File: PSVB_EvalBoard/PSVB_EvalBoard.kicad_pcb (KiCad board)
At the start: 4 copper layers, 190 x 125 mm, 453 parts, among them J10 PIN20, J11 PIN12_2x6, J12 PIN20, J13 PIN6_2x3, J2 PIN2, J29 PIN6_2x3, J3 PIN20, J30 PIN6_2x3, J31 PIN6_2x3, J4 PIN20, J5 PIN20, J6 PIN20, J7 PIN20, J8 PIN20, J9 PIN20, Q1 S9013, U1 SGM2036-ADJ, U11 93LC56BT-IOT, U12 STM32F429ZETx, U13 CH395Q, U14 CH395Q, U15 24LC64ISN, U16 MPU6050, U17 W25Q128JVSIQ, U2 SGM2036-ADJ, U3 SGM2036-ADJ, U4 INA240A1PWR, U5 INA240A1PWR, U6 TM7707, U7 REF3030, U8 REF3025, U9 REF3012, X1 2.4576Mhz, X2 12Mhz_Passive_3225, X3 16Mhz_Passive_3225, X4 30Mhz_3225, X5 30Mhz_3225

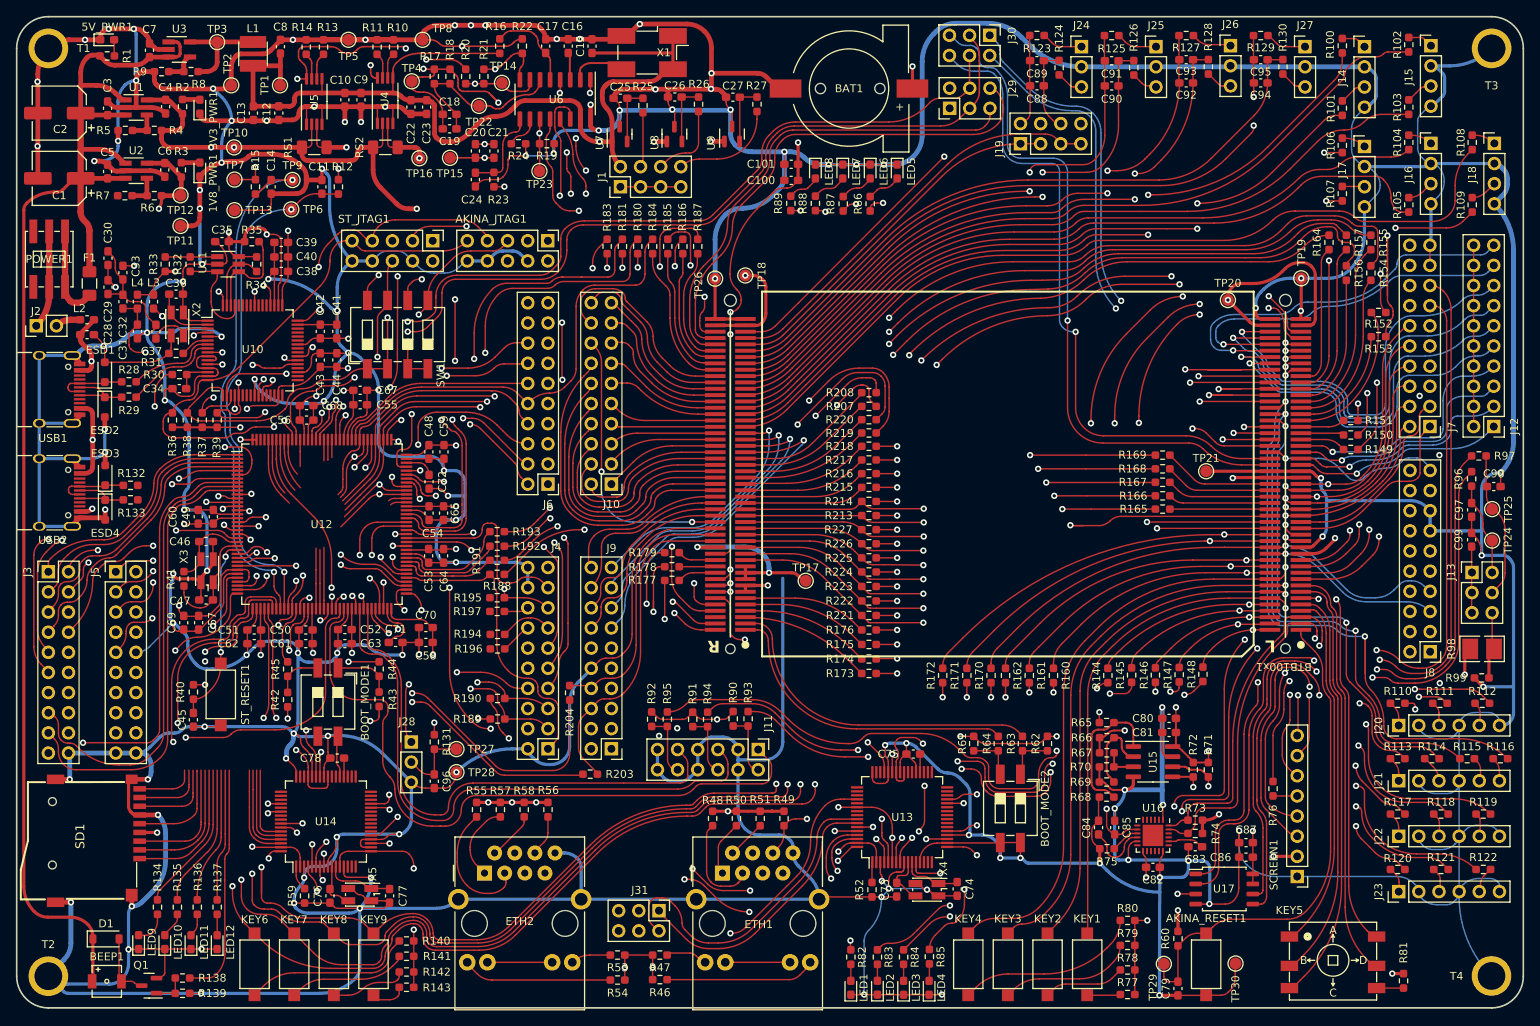
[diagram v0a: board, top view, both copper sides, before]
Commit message: 80 lines unconnected
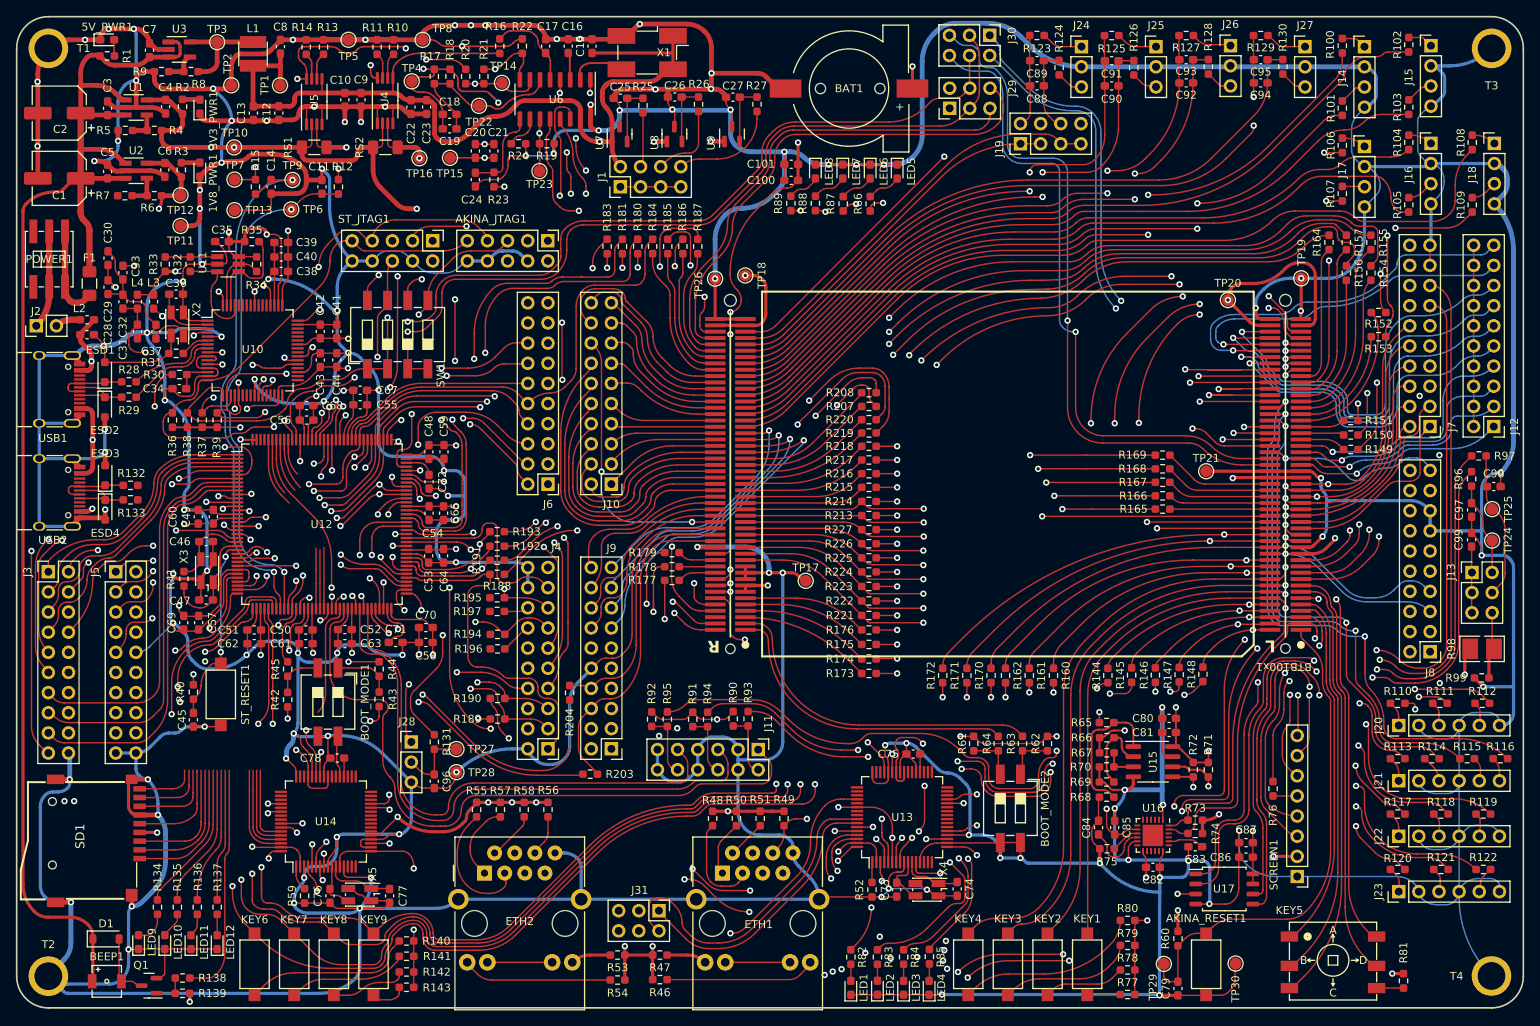
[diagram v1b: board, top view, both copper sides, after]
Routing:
- net /PC0: track 26.2 -> 212.0 mm, vias 3 -> 4
- net /PC1: track 24.1 -> 204.4 mm, vias 3 -> 4
- net /PC2: track 30.0 -> 204.1 mm, vias 3 -> 4
- net /PC13: track 49.1 -> 222.5 mm, vias 3 -> 5
- net /PE3: track 69.9 -> 242.7 mm, vias 1 -> 2
- net /PE2: track 75.1 -> 247.6 mm, vias 1 -> 2
- net /PE4: track 69.2 -> 237.7 mm, vias 1 -> 2
- net /PE5: track 68.2 -> 231.6 mm, vias 1 -> 2
- net /PC15: track 59.6 -> 221.0 mm, vias 1 -> 2
- net /PC14: track 60.7 -> 220.3 mm
- net /PE6: track 73.6 -> 231.3 mm, vias 3 -> 5
- net /PE8: track 41.0 -> 24.1 mm
- net VSS: track 2138.8 -> 2154.2 mm, vias 122 -> 121
- net /AKINA_OPA_OUT: track 7.81 -> 21.4 mm
- net /PD12: track 29.6 -> 41.9 mm, vias 1 -> 2
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
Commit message: almost finished
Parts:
- moved R173 5.60 mm to (151.9, 112.8)
- moved R174 5.60 mm to (151.9, 111.0)
- moved R175 5.60 mm to (151.9, 109.2)
- moved R176 5.60 mm to (151.9, 107.3)
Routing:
- net /PG9: track 8.85 -> 61.3 mm
- net /PG11: track 11.7 -> 63.5 mm
- net /PG10: track 13.1 -> 63.7 mm
- net /PE12: track 25.9 -> 53.8 mm, vias 2 -> 1
- net /PE10: track 26.7 -> 52.5 mm, vias 2 -> 1
- net /PG3: track 33.2 -> 58.0 mm, vias 2 -> 1
- net /PE8: track 24.1 -> 48.5 mm, vias 2 -> 1
- net /PE7: track 44.8 -> 67.1 mm, vias 2 -> 1
- net /PG6: track 41.9 -> 62.2 mm, vias 3 -> 2
- net /PG2: track 29.8 -> 49.5 mm, vias 1 -> 0
- net /PG5: track 41.8 -> 60.1 mm, vias 2 -> 1
- net /AD3: track 101.1 -> 118.2 mm, vias 5 -> 6
- net /BTB_PG0: track 71.8 -> 55.0 mm
- net /PG1: track 37.2 -> 53.9 mm, vias 2 -> 1
- net /PG4: track 44.8 -> 60.2 mm, vias 4 -> 3
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
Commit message: i need one day more
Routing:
- net +1V8: track 223.8 -> 341.0 mm, vias 15 -> 17
- net /FT_USART4_RX: track 48.4 -> 114.3 mm, vias 1 -> 2
- net /FT_USART4_TX: track 54.4 -> 114.4 mm, vias 1 -> 2
- net /PC9: track 47.2 -> 95.4 mm, vias 2 -> 3
- net /PC8: track 45.8 -> 91.8 mm, vias 2 -> 3
- net /PD3: track 72.2 -> 117.1 mm, vias 4 -> 5
- net /STM32_ETH_SDI: track 13.7 -> 55.7 mm, vias 1 -> 3
- net /PC12: track 58.2 -> 99.4 mm, vias 2 -> 3
- net /PC11: track 60.5 -> 100.7 mm, vias 2 -> 3
- net /PD2: track 54.3 -> 94.1 mm, vias 3 -> 4
- net /PB8: track 25.2 -> 64.7 mm, vias 0 -> 2
- net /PB6: track 23.2 -> 62.5 mm, vias 0 -> 2
- net /PC10: track 59.7 -> 98.9 mm, vias 2 -> 3
- net /STM32_ETH_SCK: track 13.5 -> 51.9 mm, vias 1 -> 2
- net /PB7: track 23.9 -> 62.2 mm, vias 0 -> 2
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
